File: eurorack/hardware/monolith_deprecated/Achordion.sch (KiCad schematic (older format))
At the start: 120 parts, among them J1 Power, J10 Jack, J11 Jack, J2 Serial, J3 SWD, J4 Jack, J5 Jack, J6 Jack, J7 Jack, J8 Jack, J9 Jack, SW2 Button, U1 STM32F405RGT6, U10 SC39-11SURKWA, U2 LM1117-3.3, U3 LM1117-3.3, U4 LM4040C10, U5 TLV320AIC23BPW, U6 TL072, U7 MCP6002, U8 MCP6002, U9 MCP6002, Y1 8MHz

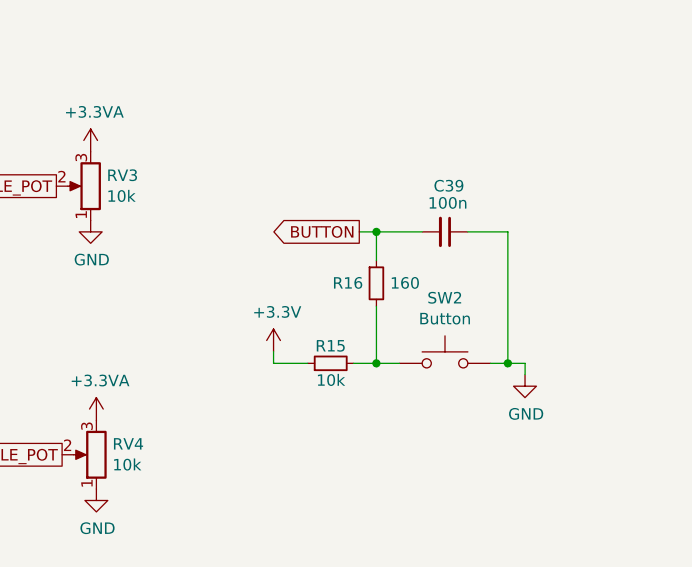
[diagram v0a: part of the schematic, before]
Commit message: Move harware to its own directory
JLCPCB does not offer the MCU this was designed for. I'm starting again,
this time making the design modular.

Signed-off-by: Petr Horacek <hrck@protonmail.com>
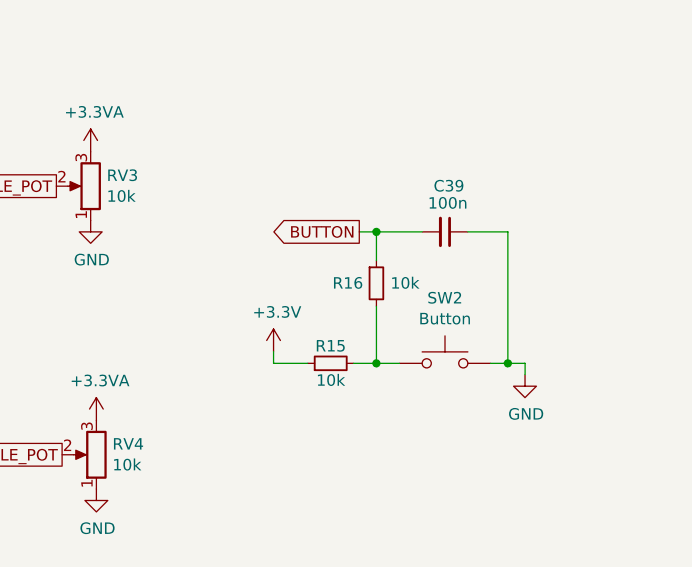
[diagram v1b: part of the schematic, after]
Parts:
- C1, C2: LCSC Part # (none) -> C23630
- C10: LCSC Part # (none) -> C15195
- C11, C12: LCSC Part # (none) -> C1547
- C13, C16, C21: LCSC Part # (none) -> C24497
- C14, C17, C23: LCSC Part # (none) -> C129272
- C15, C18, C22, C25, C27, C29, C31, C32, C39, C4, C5, C6, C7, C8: LCSC Part # (none) -> C1525
- C19, C20: LCSC Part # (none) -> C122226
- C24, C26, C28, C30, C35, C37: LCSC Part # (none) -> C7171
- C3: LCSC Part # (none) -> C19666
- C33, C34: LCSC Part # (none) -> C14663
- C36, C38: LCSC Part # (none) -> C1647
- C40, C41, C42, C43, C44, C45, C46, C47, C48: LCSC Part # (none) -> C1613
- C9: LCSC Part # (none) -> C15849
- D1, D2: LCSC Part # (none) -> C8598
- FB1, FB2: LCSC Part # (none) -> C341252
- R10, R14, R4, R5: LCSC Part # (none) -> C21190
- R11, R13, R19, R29, R7, R9: LCSC Part # (none) -> C25819
- R12, R8: LCSC Part # (none) -> C23212
- R15: LCSC Part # (none) -> C25744
- R16: value 160 -> 10k; LCSC Part # (none) -> C25744
- R17, R27: LCSC Part # (none) -> C22827
- R18, R21, R25, R28, R30, R33: LCSC Part # (none) -> C25803
- R2, R3: LCSC Part # (none) -> C25879
- R20, R23, R24, R32: LCSC Part # (none) -> C25808
- R22, R26, R31, R34: LCSC Part # (none) -> C4184
- R35, R36, R37, R38, R39, R40, R41, R42: LCSC Part # (none) -> C23032
- R6: LCSC Part # (none) -> C25092
- U2, U3: LCSC Part # (none) -> C19228
- U4: LCSC Part # (none) -> C201738
- U5: LCSC Part # (none) -> C9915
- U6: LCSC Part # (none) -> C163525
- U7, U8, U9: LCSC Part # (none) -> C7377
